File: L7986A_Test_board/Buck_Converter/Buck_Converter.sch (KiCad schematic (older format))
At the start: 17 parts, among them IC1 L7986A

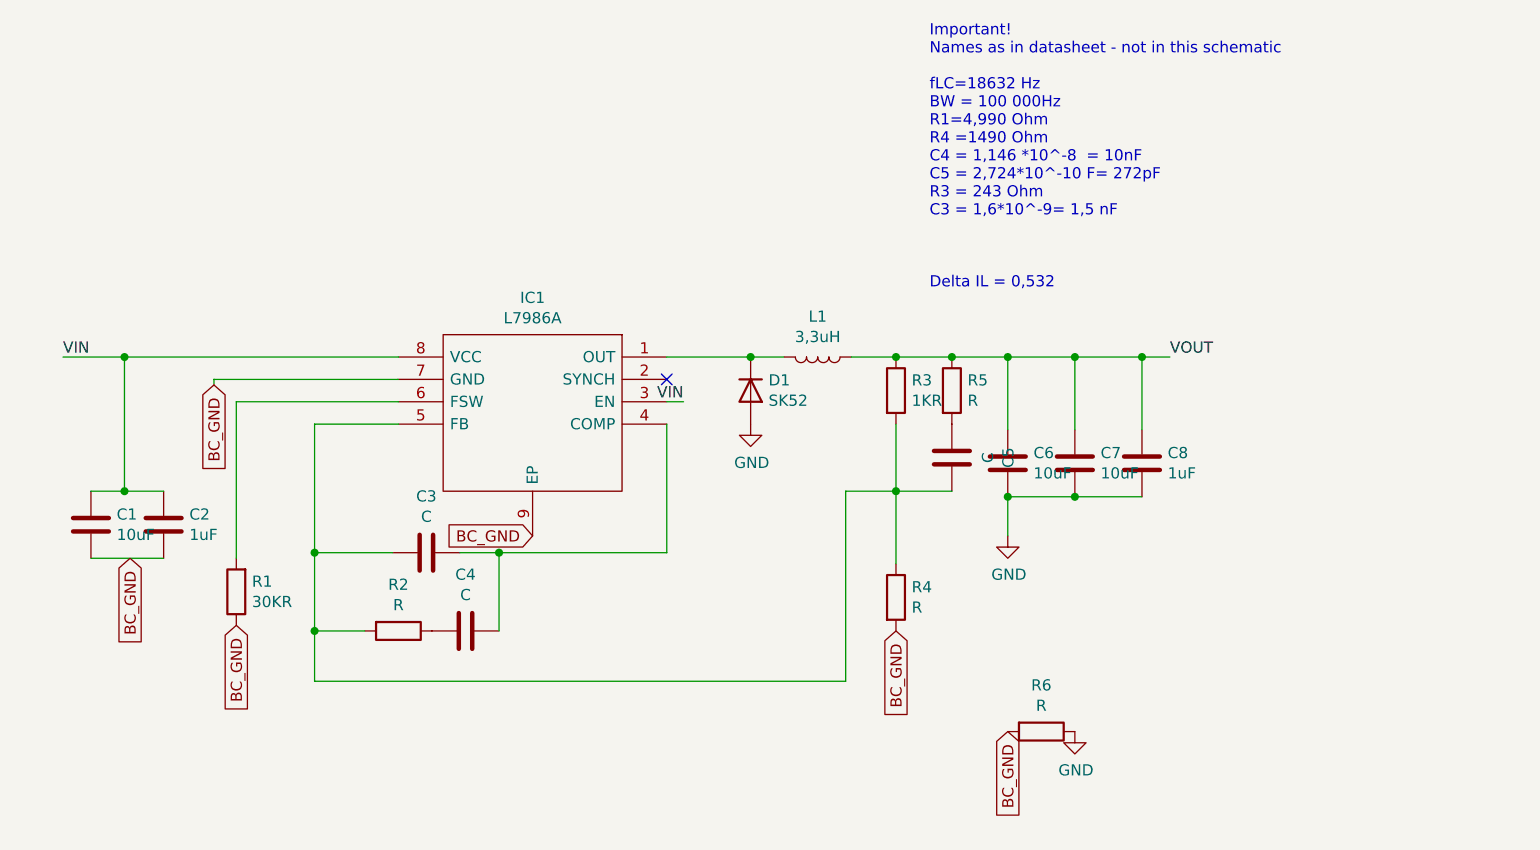
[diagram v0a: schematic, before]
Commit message: Board zones added
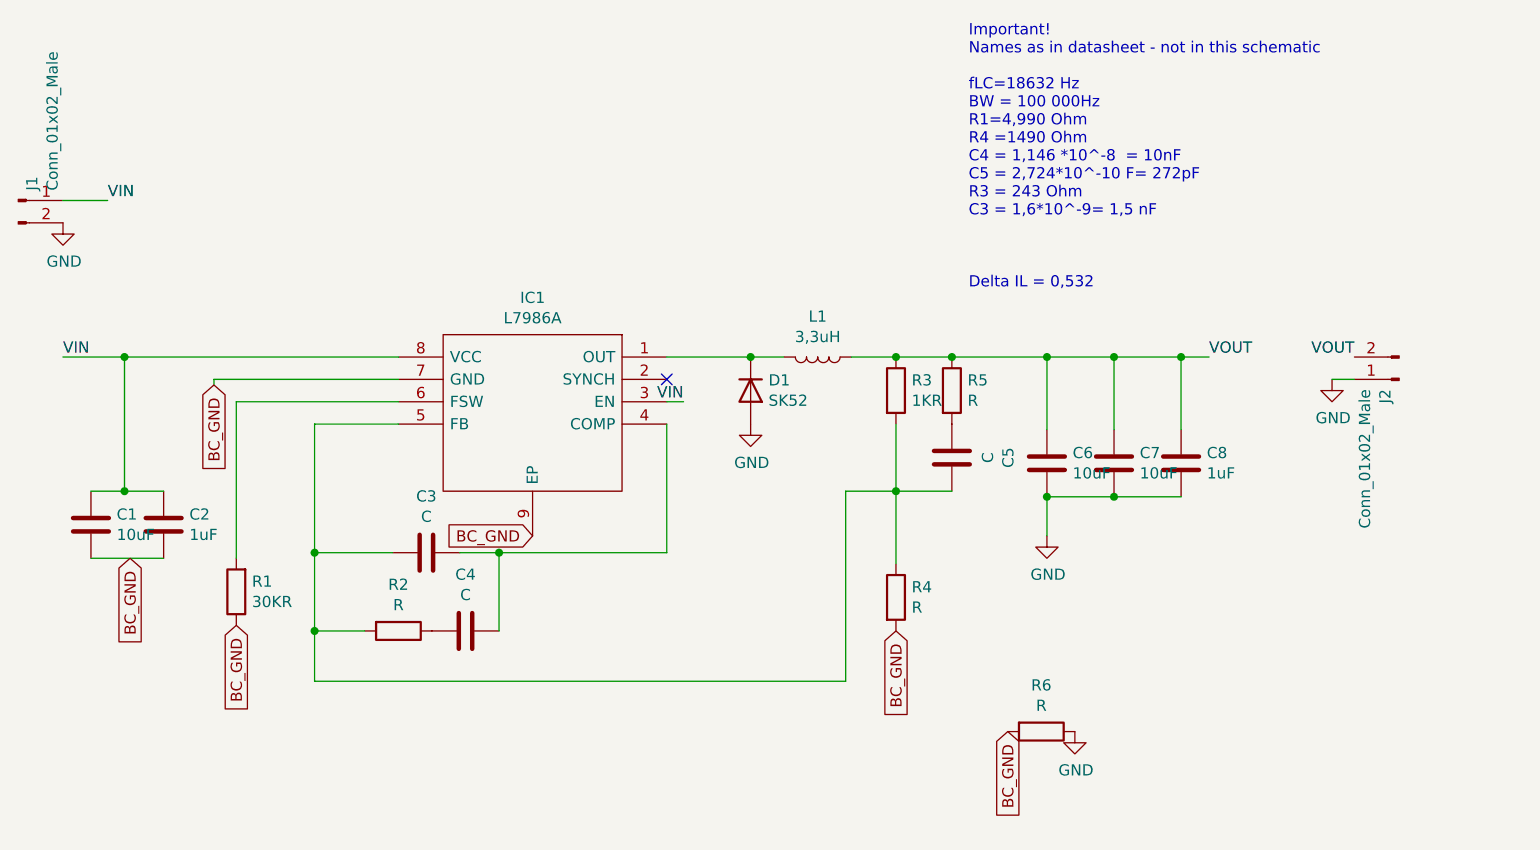
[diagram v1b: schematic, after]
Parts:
- added J1, J2: Conn_01x02_Male, Diode_THT:D_T-1_P2.54mm_Vertical_AnodeUp, symbol Connector:Conn_01x02_Male
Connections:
- net GND: now also J1.2 (Pin_2), J2.1 (Pin_1)
- net VIN: now also J1.1 (Pin_1)
- net VOUT: now also J2.2 (Pin_2)
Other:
- moved on the sheet: C6, C7, C8
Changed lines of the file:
@@
 L Device:C C6
 U 1 1 6090FC52
-P 5275 3875
-F 0 "C6" H 5160 3829 50  0000 R CNN
-F 1 "10uF" H 5160 3920 50  0000 R CNN
-F 2 "Capacitor_SMD:C_1206_3216Metric" H 5313 3725 50  0001 C CNN
-F 3 "~" H 5275 3875 50  0001 C CNN
-	1    5275 3875
-	-1   0    0    1
-$EndComp
-Wire Wire Line
-	5275 3725 5275 3400
-Wire Wire Line
-	5275 3400 5025 3400
+P 5450 3875
+F 0 "C6" H 5335 3829 50  0000 R CNN
+F 1 "10uF" H 5335 3920 50  0000 R CNN
+F 2 "Capacitor_SMD:C_1206_3216Metric" H 5488 3725 50  0001 C CNN
+F 3 "~" H 5450 3875 50  0001 C CNN
+	1    5450 3875
+	-1   0    0    1
+$EndComp
+Wire Wire Line
+	5450 3725 5450 3400
 Connection ~ 4775 3400
 Wire Wire Line
@@
 L power:GND #PWR0106
 U 1 1 60910962
-P 5275 4200
-F 0 "#PWR0106" H 5275 3950 50  0001 C CNN
-F 1 "GND" H 5280 4027 50  0000 C CNN
-F 2 "" H 5275 4200 50  0001 C CNN
-F 3 "" H 5275 4200 50  0001 C CNN
-	1    5275 4200
-	1    0    0    -1
-$EndComp
-Wire Wire Line
-	5275 4200 5275 4025
+P 5450 4200
+F 0 "#PWR0106" H 5450 3950 50  0001 C CNN
+F 1 "GND" H 5455 4027 50  0000 C CNN
+F 2 "" H 5450 4200 50  0001 C CNN
+F 3 "" H 5450 4200 50  0001 C CNN
+	1    5450 4200
+	1    0    0    -1
+$EndComp
+Wire Wire Line
+	5450 4200 5450 4025
 Wire Wire Line
 	4550 4850 2175 4850
@@
 	2175 4850 2175 4625
 Connection ~ 2175 4625
-Text Label 6000 3400 0    50   ~ 0
+Text Label 6175 3400 0    50   ~ 0
 VOUT
 $Comp
@@
 Wire Wire Line
 	1325 4000 1175 4000
-Text Notes 4925 3100 0    50   ~ 0
+Text Notes 5100 3100 0    50   ~ 0
 Important!\nNames as in datasheet - not in this schematic\n\nfLC=18632 Hz\nBW = 100 000Hz\nR1=4,990 Ohm\nR4 =1490 Ohm\nC4 = 1,146 *10^-8  = 10nF\nC5 = 2,724*10^-10 F= 272pF\nR3 = 243 Ohm\nC3 = 1,6*10^-9= 1,5 nF\n\n\n\nDelta IL = 0,532\n
 Wire Wire Line
-	6000 3400 5875 3400
-Connection ~ 5275 3400
-Wire Wire Line
-	5575 3725 5575 3400
-Connection ~ 5575 3400
-Wire Wire Line
-	5575 3400 5275 3400
-Wire Wire Line
-	5875 3725 5875 3400
-Connection ~ 5875 3400
-Wire Wire Line
-	5875 3400 5575 3400
-Connection ~ 5275 4025
+	6175 3400 6050 3400
+Connection ~ 5450 3400
+Wire Wire Line
+	5750 3725 5750 3400
+Connection ~ 5750 3400
+Wire Wire Line
+	5750 3400 5450 3400
+Wire Wire Line
+	6050 3725 6050 3400
+Connection ~ 6050 3400
+Wire Wire Line
+	6050 3400 5750 3400
+Connection ~ 5450 4025
 $Comp
 L Device:C C7
 U 1 1 60915445
-P 5575 3875
-F 0 "C7" H 5460 3829 50  0000 R CNN
-F 1 "10uF" H 5460 3920 50  0000 R CNN
-F 2 "Capacitor_SMD:C_1206_3216Metric" H 5613 3725 50  0001 C CNN
-F 3 "~" H 5575 3875 50  0001 C CNN
-	1    5575 3875
-	-1   0    0    1
-$EndComp
-Wire Wire Line
-	5275 4025 5575 4025
-Connection ~ 5575 4025
-Wire Wire Line
-	5575 4025 5875 4025
+P 5750 3875
+F 0 "C7" H 5635 3829 50  0000 R CNN
+F 1 "10uF" H 5635 3920 50  0000 R CNN
+F 2 "Capacitor_SMD:C_1206_3216Metric" H 5788 3725 50  0001 C CNN
+F 3 "~" H 5750 3875 50  0001 C CNN
+	1    5750 3875
+	-1   0    0    1
+$EndComp
+Wire Wire Line
+	5450 4025 5750 4025
+Connection ~ 5750 4025
+Wire Wire Line
+	5750 4025 6050 4025
 $Comp
 L Device:C C8
 U 1 1 609159DF
-P 5875 3875
-F 0 "C8" H 5760 3829 50  0000 R CNN
-F 1 "1uF" H 5760 3920 50  0000 R CNN
-F 2 "Capacitor_SMD:C_1206_3216Metric" H 5913 3725 50  0001 C CNN
-F 3 "~" H 5875 3875 50  0001 C CNN
-	1    5875 3875
+P 6050 3875
+F 0 "C8" H 5935 3829 50  0000 R CNN
+F 1 "1uF" H 5935 3920 50  0000 R CNN
+F 2 "Capacitor_SMD:C_1206_3216Metric" H 6088 3725 50  0001 C CNN
+F 3 "~" H 6050 3875 50  0001 C CNN
+	1    6050 3875
 	-1   0    0    1
 $EndComp
@@
 	1    0    0    -1
 $EndComp
-Connection ~ 5025 3400
 Wire Wire Line
 	5025 3400 4775 3400
@@
 Text GLabel 1725 3525 3    50   Input ~ 0
 BC_GND
+Wire Wire Line
+	5025 3400 5450 3400
+Connection ~ 5025 3400
+$Comp
+L Connector:Conn_01x02_Male J2
+U 1 1 60976C7B
+P 7025 3500
+F 0 "J2" V 7087 3544 50  0000 L CNN
+F 1 "Conn_01x02_Male" V 7178 3544 50  0000 L CNN
+F 2 "Diode_THT:D_T-1_P2.54mm_Vertical_AnodeUp" H 7025 3500 50  0001 C CNN
+F 3 "~" H 7025 3500 50  0001 C CNN
+	1    7025 3500
+	-1   0    0    1
+$EndComp
+Text Label 6825 3400 2    50   ~ 0
+VOUT
+$Comp
+L power:GND #PWR0101
+U 1 1 60979499
+P 6725 3500
+F 0 "#PWR0101" H 6725 3250 50  0001 C CNN
+F 1 "GND" H 6730 3327 50  0000 C CNN
+F 2 "" H 6725 3500 50  0001 C CNN
+F 3 "" H 6725 3500 50  0001 C CNN
+	1    6725 3500
+	1    0    0    -1
+$EndComp
+Wire Wire Line
+	6725 3500 6825 3500
+$Comp
+L Connector:Conn_01x02_Male J1
+U 1 1 6097A326
+P 850 2700
+F 0 "J1" V 912 2744 50  0000 L CNN
+F 1 "Conn_01x02_Male" V 1003 2744 50  0000 L CNN
+F 2 "Diode_THT:D_T-1_P2.54mm_Vertical_AnodeUp" H 850 2700 50  0001 C CNN
+F 3 "~" H 850 2700 50  0001 C CNN
+	1    850  2700
+	1    0    0    -1
+$EndComp
+Text Label 1250 2700 0    50   ~ 0
+VIN
+Wire Wire Line
+	1250 2700 1050 2700
+$Comp
+L power:GND #PWR0102
+U 1 1 6097BDF8
+P 1050 2800
+F 0 "#PWR0102" H 1050 2550 50  0001 C CNN
+F 1 "GND" H 1055 2627 50  0000 C CNN
+F 2 "" H 1050 2800 50  0001 C CNN
+F 3 "" H 1050 2800 50  0001 C CNN
+	1    1050 2800
+	1    0    0    -1
+$EndComp
 $EndSCHEMATC

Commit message: Filled zones fixed
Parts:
- J1, J2: footprint Diode_THT:D_T-1_P2.54mm_Vertical_AnodeUp -> Connector_PinHeader_2.54mm:PinHeader_1x02_P2.54mm_Vertical
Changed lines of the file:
@@
 F 0 "J2" V 7087 3544 50  0000 L CNN
 F 1 "Conn_01x02_Male" V 7178 3544 50  0000 L CNN
-F 2 "Diode_THT:D_T-1_P2.54mm_Vertical_AnodeUp" H 7025 3500 50  0001 C CNN
+F 2 "Connector_PinHeader_2.54mm:PinHeader_1x02_P2.54mm_Vertical" H 7025 3500 50  0001 C CNN
 F 3 "~" H 7025 3500 50  0001 C CNN
 	1    7025 3500
@@
 F 0 "J1" V 912 2744 50  0000 L CNN
 F 1 "Conn_01x02_Male" V 1003 2744 50  0000 L CNN
-F 2 "Diode_THT:D_T-1_P2.54mm_Vertical_AnodeUp" H 850 2700 50  0001 C CNN
+F 2 "Connector_PinHeader_2.54mm:PinHeader_1x02_P2.54mm_Vertical" H 850 2700 50  0001 C CNN
 F 3 "~" H 850 2700 50  0001 C CNN
 	1    850  2700

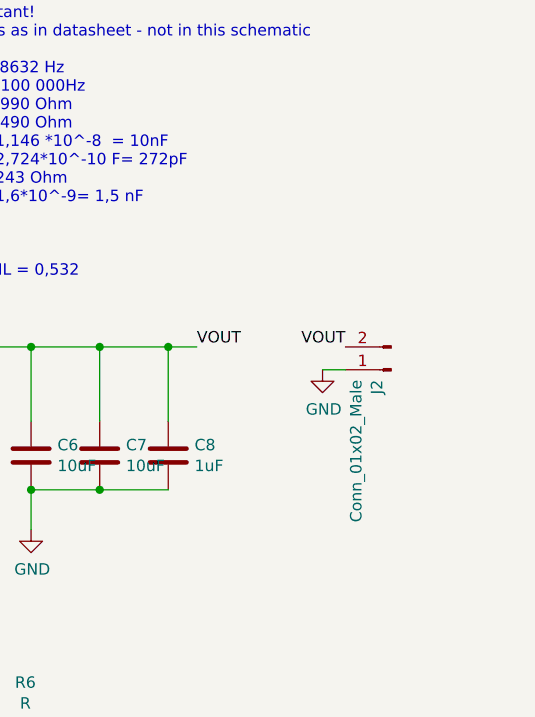
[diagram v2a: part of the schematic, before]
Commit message: Labels Fixed
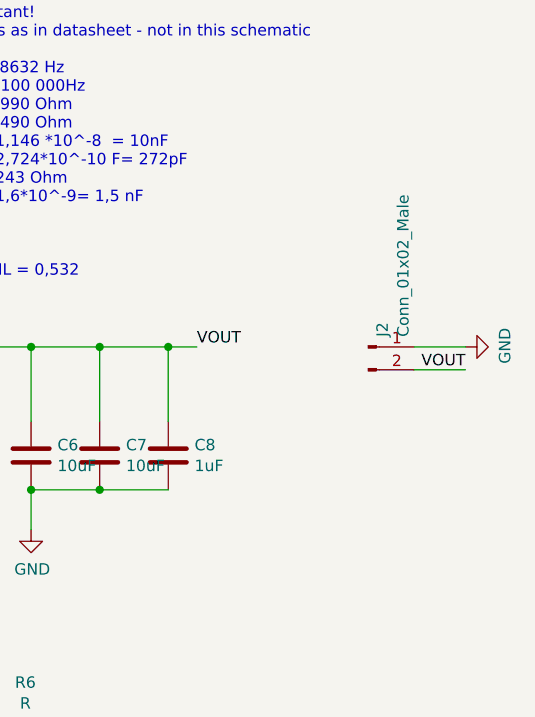
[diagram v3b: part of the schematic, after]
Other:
- moved on the sheet: J2
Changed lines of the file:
@@
 L Connector:Conn_01x02_Male J2
 U 1 1 60976C7B
-P 7025 3500
-F 0 "J2" V 7087 3544 50  0000 L CNN
-F 1 "Conn_01x02_Male" V 7178 3544 50  0000 L CNN
-F 2 "Connector_PinHeader_2.54mm:PinHeader_1x02_P2.54mm_Vertical" H 7025 3500 50  0001 C CNN
-F 3 "~" H 7025 3500 50  0001 C CNN
-	1    7025 3500
-	-1   0    0    1
+P 6925 3400
+F 0 "J2" V 6987 3444 50  0000 L CNN
+F 1 "Conn_01x02_Male" V 7078 3444 50  0000 L CNN
+F 2 "Connector_PinHeader_2.54mm:PinHeader_1x02_P2.54mm_Vertical" H 6925 3400 50  0001 C CNN
+F 3 "~" H 6925 3400 50  0001 C CNN
+	1    6925 3400
+	1    0    0    -1
 $EndComp
-Text Label 6825 3400 2    50   ~ 0
-VOUT
 $Comp
 L power:GND #PWR0101
 U 1 1 60979499
-P 6725 3500
-F 0 "#PWR0101" H 6725 3250 50  0001 C CNN
-F 1 "GND" H 6730 3327 50  0000 C CNN
-F 2 "" H 6725 3500 50  0001 C CNN
-F 3 "" H 6725 3500 50  0001 C CNN
-	1    6725 3500
-	1    0    0    -1
+P 7350 3400
+F 0 "#PWR0101" H 7350 3150 50  0001 C CNN
+F 1 "GND" H 7355 3227 50  0000 C CNN
+F 2 "" H 7350 3400 50  0001 C CNN
+F 3 "" H 7350 3400 50  0001 C CNN
+	1    7350 3400
+	0    -1   -1   0
 $EndComp
-Wire Wire Line
-	6725 3500 6825 3500
 $Comp
 L Connector:Conn_01x02_Male J1
@@
 	1    0    0    -1
 $EndComp
+Wire Wire Line
+	7350 3400 7125 3400
+Wire Wire Line
+	7350 3500 7125 3500
+Text Label 7350 3500 2    50   ~ 0
+VOUT
 $EndSCHEMATC
